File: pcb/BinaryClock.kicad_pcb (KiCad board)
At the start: 2 copper layers, 28.4 x 41.7 mm, 20 parts, among them CON1 AVR-ISP-6, CON2 BARREL_JACK, U1 MC33269, U2 DS3231, U3 clock_header, U4 clock_header, U6 ATMEGA328-AU, Y1 16MHz

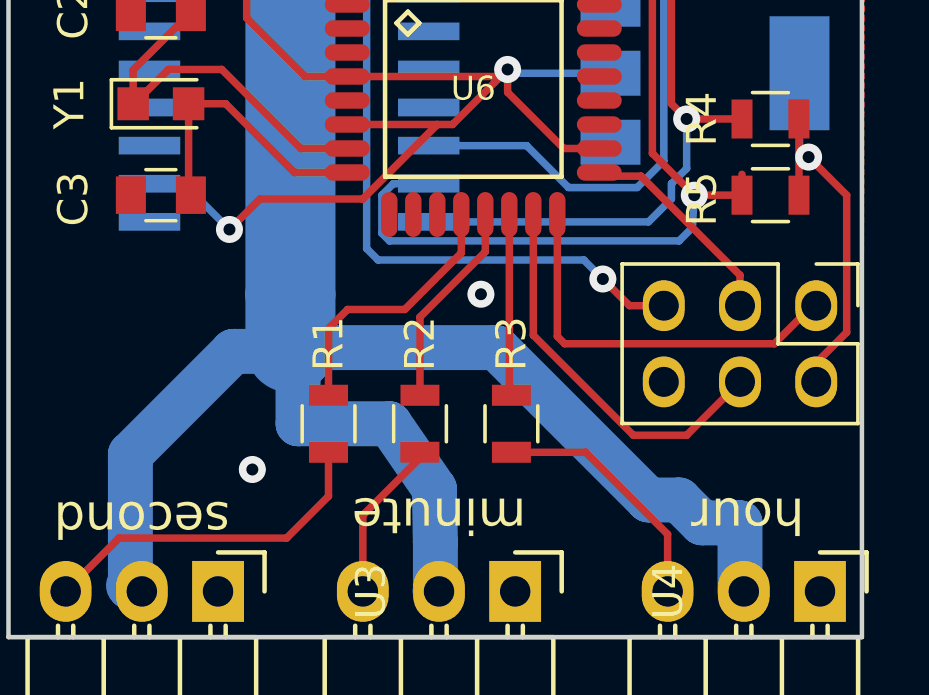
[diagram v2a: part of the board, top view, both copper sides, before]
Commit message: Hack to connect vias to ground plane.
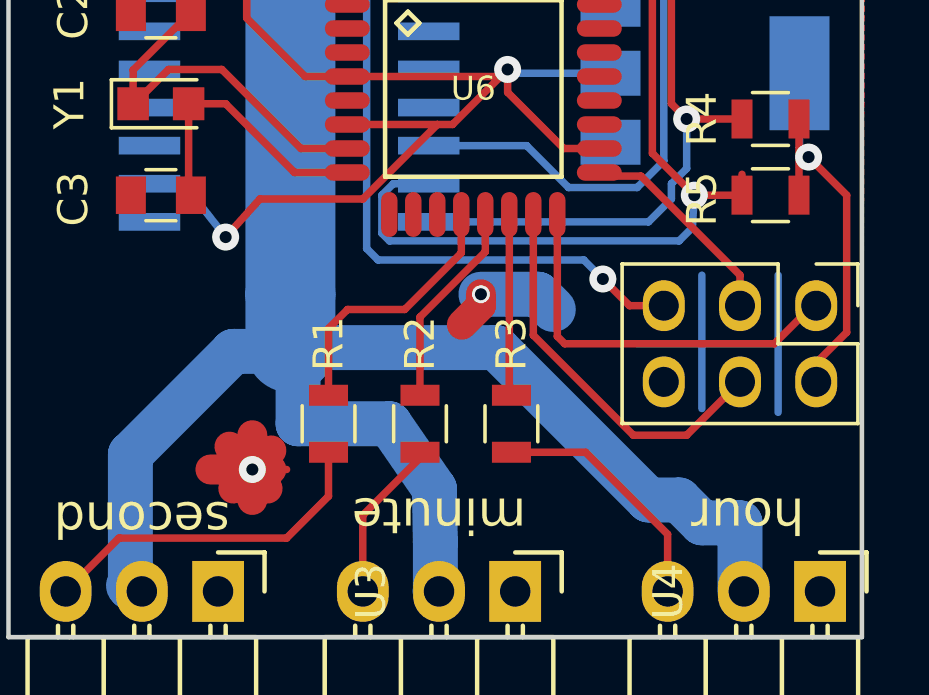
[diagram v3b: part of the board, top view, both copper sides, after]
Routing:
- net (no net): track 0.00 -> 37.8 mm
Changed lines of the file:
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@@
   (general
     (links 55)
-    (no_connects 9)
+    (no_connects 10)
     (area 143.688999 56.820999 172.287001 98.627001)
     (thickness 1.6)
     (drawings 14)
-    (tracks 165)
+    (tracks 199)
     (zones 0)
     (modules 20)
@@
   )
   (setup
-    (last_trace_width 0.25)
+    (last_trace_width 1)
+    (user_trace_width 1)
     (user_trace_width 1.5)
     (user_trace_width 3)
@@
   (gr_line (start 172.212 56.896) (end 145.796 56.896) (angle 90) (layer Edge.Cuts) (width 0.15))
   (gr_line (start 172.212 98.552) (end 172.212 56.896) (angle 90) (layer Edge.Cuts) (width 0.15))
-  (via (at 159.512 87.122) (size 0.9) (drill 0.4) (layers F.Cu B.Cu) (net 0))
+  (segment (start 151.892 92.964) (end 151.511 92.583) (width 1) (layer B.Cu) (net 0))
+  (segment (start 151.892 92.964) (end 151.384 93.472) (width 1) (layer B.Cu) (net 0))
+  (segment (start 151.892 92.964) (end 152.273 92.583) (width 1) (layer B.Cu) (net 0))
+  (segment (start 152.273 92.583) (end 151.892 92.964) (width 1) (layer B.Cu) (net 0))
+  (segment (start 151.892 92.964) (end 152.273 93.345) (width 1) (layer B.Cu) (net 0))
+  (segment (start 151.892 92.964) (end 152.908 92.964) (width 0.25) (layer B.Cu) (net 0))
+  (segment (start 150.749 92.964) (end 151.892 92.964) (width 0.25) (layer B.Cu) (net 0))
+  (segment (start 151.892 92.964) (end 151.892 93.091) (width 1) (layer F.Cu) (net 0))
+  (segment (start 151.892 93.091) (end 152.4 93.599) (width 1) (layer F.Cu) (net 0))
+  (segment (start 151.892 92.964) (end 151.257 93.599) (width 1) (layer F.Cu) (net 0))
+  (segment (start 151.892 92.964) (end 152.527 92.329) (width 1) (layer F.Cu) (net 0))
+  (segment (start 151.892 92.964) (end 151.892 93.98) (width 1) (layer F.Cu) (net 0))
+  (segment (start 151.892 92.964) (end 151.892 93.98) (width 0.25) (layer F.Cu) (net 0))
+  (segment (start 151.892 92.964) (end 152.527 92.964) (width 1) (layer F.Cu) (net 0))
+  (segment (start 151.892 92.964) (end 151.13 92.202) (width 1) (layer F.Cu) (net 0))
+  (segment (start 151.892 92.964) (end 151.892 91.821) (width 1) (layer F.Cu) (net 0))
+  (segment (start 151.892 92.964) (end 151.892 91.821) (width 0.25) (layer F.Cu) (net 0))
+  (segment (start 151.892 92.964) (end 150.495 92.964) (width 1) (layer F.Cu) (net 0))
+  (segment (start 159.512 87.122) (end 159.512 87.503) (width 1) (layer F.Cu) (net 0))
+  (segment (start 159.512 87.503) (end 158.877 88.138) (width 1) (layer F.Cu) (net 0))
+  (segment (start 159.512 87.122) (end 159.512 88.011) (width 0.25) (layer F.Cu) (net 0))
+  (segment (start 159.512 88.011) (end 159.258 88.265) (width 0.25) (layer F.Cu) (net 0))
+  (segment (start 159.512 87.122) (end 161.417 87.122) (width 1.5) (layer B.Cu) (net 0))
+  (via (at 159.512 87.122) (size 0.6) (drill 0.4) (layers F.Cu B.Cu) (net 0))
+  (segment (start 161.925 87.63) (end 161.417 87.122) (width 1.5) (layer B.Cu) (net 0))
+  (segment (start 152.527 92.964) (end 153.035 92.964) (width 0.25) (layer F.Cu) (net 0))
+  (segment (start 151.892 92.964) (end 150.749 92.964) (width 0.25) (layer F.Cu) (net 0))
   (via (at 151.892 92.964) (size 0.9) (drill 0.4) (layers F.Cu B.Cu) (net 0))
+  (segment (start 151.892 92.964) (end 151.892 93.98) (width 0.25) (layer B.Cu) (net 0))
+  (segment (start 151.892 92.964) (end 151.892 91.821) (width 0.25) (layer B.Cu) (net 0))
+  (segment (start 166.878 88.773) (end 169.418 88.773) (width 0.25) (layer B.Cu) (net 0))
+  (segment (start 164.719 88.773) (end 166.878 88.773) (width 0.25) (layer B.Cu) (net 0))
+  (segment (start 169.418 91.059) (end 169.418 88.773) (width 0.25) (layer B.Cu) (net 0))
+  (segment (start 169.418 88.773) (end 169.418 86.487) (width 0.25) (layer B.Cu) (net 0))
+  (segment (start 166.878 90.932) (end 166.878 88.773) (width 0.25) (layer B.Cu) (net 0))
+  (segment (start 166.878 88.773) (end 166.878 86.487) (width 0.25) (layer B.Cu) (net 0))
   (segment (start 147.919 80.772) (end 147.955 80.772) (width 0.25) (layer F.Cu) (net 2))
   (segment (start 147.955 80.772) (end 149.098 79.629) (width 0.25) (layer F.Cu) (net 2))
@@
   (segment (start 155.575 83.947) (end 158.058 81.464) (width 0.25) (layer F.Cu) (net 7))
   (segment (start 152.146 83.947) (end 155.575 83.947) (width 0.25) (layer F.Cu) (net 7))
-  (segment (start 151.13 84.963) (end 152.146 83.947) (width 0.25) (layer F.Cu) (net 7))
-  (via (at 151.13 84.963) (size 0.9) (drill 0.4) (layers F.Cu B.Cu) (net 7))
-  (segment (start 149.606 83.439) (end 151.13 84.963) (width 0.25) (layer B.Cu) (net 7))
+  (segment (start 151.003 85.217) (end 152.146 83.947) (width 0.25) (layer F.Cu) (net 7))
+  (via (at 151.003 85.217) (size 0.9) (drill 0.4) (layers F.Cu B.Cu) (net 7))
+  (segment (start 149.606 83.439) (end 151.003 85.217) (width 0.25) (layer B.Cu) (net 7))
   (segment (start 170.688 90.043) (end 170.688 89.408) (width 0.25) (layer F.Cu) (net 7))
   (segment (start 170.688 89.408) (end 171.704 88.392) (width 0.25) (layer F.Cu) (net 7))
